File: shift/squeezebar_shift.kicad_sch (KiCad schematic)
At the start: 54 parts, among them J0 OUTR, J1 PNK, J10 I2C, J11 IDC, J2 RNG, J3 MID, J4 IDX, J5 INNR, J6 THM, J7 XTR, J8 ENCODER, U1 74HC164

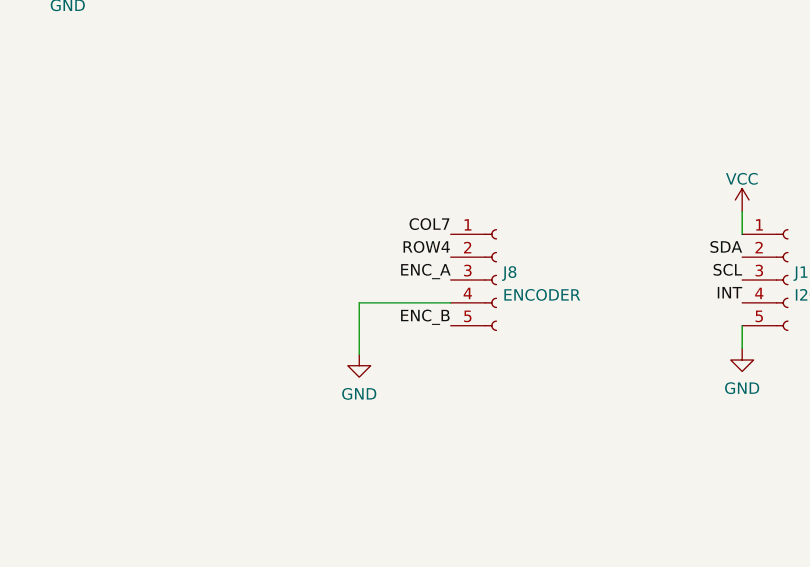
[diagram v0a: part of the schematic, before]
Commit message: Add SqueezeBarrel
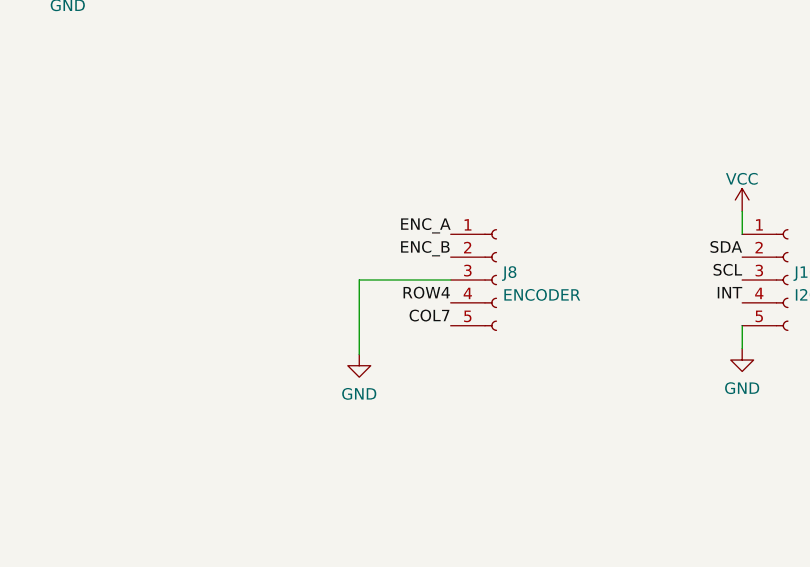
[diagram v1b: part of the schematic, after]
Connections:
- net COL7: now also J8.5 (Pin_5); no longer J8.1 (Pin_1)
- net ENC_A: now also J8.1 (Pin_1); no longer J8.3 (Pin_3)
- net ENC_B: now also J8.2 (Pin_2); no longer J8.5 (Pin_5)
- net GND: now also J8.3 (Pin_3); no longer J8.4 (Pin_4)
- net ROW4: now also J8.4 (Pin_4); no longer J8.2 (Pin_2)
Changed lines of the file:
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@@
     (stroke (width 0) (type default) (color 0 0 0 0))
   )
-  (wire (pts (xy 74.93 92.71) (xy 74.93 98.425))
+  (wire (pts (xy 74.93 90.17) (xy 74.93 98.425))
     (stroke (width 0) (type default) (color 0 0 0 0))
   )
@@
     (stroke (width 0) (type default) (color 0 0 0 0))
   )
-  (wire (pts (xy 85.09 92.71) (xy 74.93 92.71))
+  (wire (pts (xy 85.09 90.17) (xy 74.93 90.17))
     (stroke (width 0) (type default) (color 0 0 0 0))
   )
@@
     (effects (font (size 1.27 1.27)) (justify right bottom))
   )
-  (label "ROW4" (at 85.09 87.63 180)
+  (label "ROW4" (at 85.09 92.71 180)
     (effects (font (size 1.27 1.27)) (justify right bottom))
   )
@@
     (effects (font (size 1.27 1.27)) (justify left bottom))
   )
-  (label "ENC_A" (at 85.09 90.17 180)
+  (label "ENC_A" (at 85.09 85.09 180)
     (effects (font (size 1.27 1.27)) (justify right bottom))
   )
@@
     (effects (font (size 1.27 1.27)) (justify left bottom))
   )
-  (label "COL7" (at 85.09 85.09 180)
+  (label "COL7" (at 85.09 95.25 180)
     (effects (font (size 1.27 1.27)) (justify right bottom))
   )
@@
     (effects (font (size 1.27 1.27)) (justify left bottom))
   )
-  (label "ENC_B" (at 85.09 95.25 180)
-    (effects (font (size 1.27 1.27)) (justify right bottom))
-  )
+  (label "ENC_B" (at 85.09 87.63 180)
+    (effects (font (size 1.27 1.27)) (justify right bottom))
+  )
